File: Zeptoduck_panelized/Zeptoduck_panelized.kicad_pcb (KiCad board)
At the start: 2 copper layers, 23.9 x 37 mm, 110 parts, among them J2 USB4151-GF-C, U1 ATSAMD11D14A-U, U2 TLV73333PDQNR

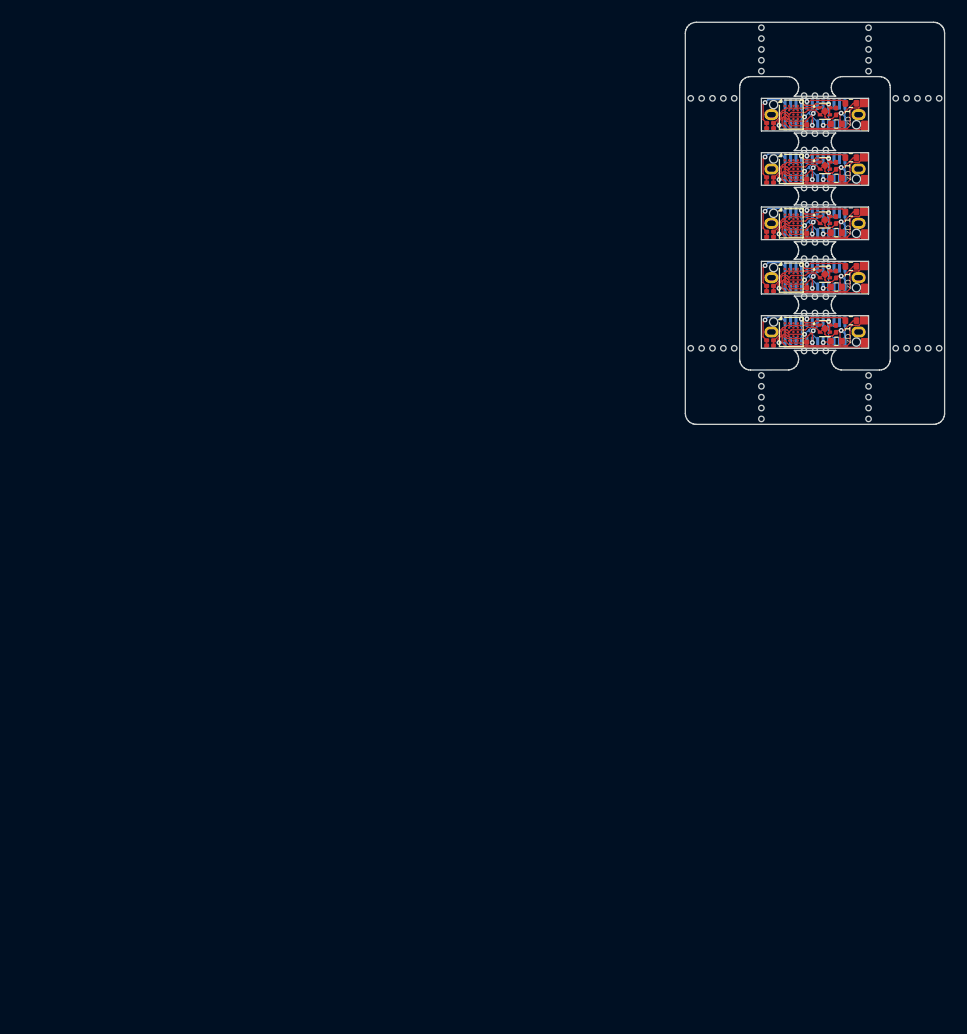
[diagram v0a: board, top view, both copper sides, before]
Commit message: Updated and fixed the Panelization
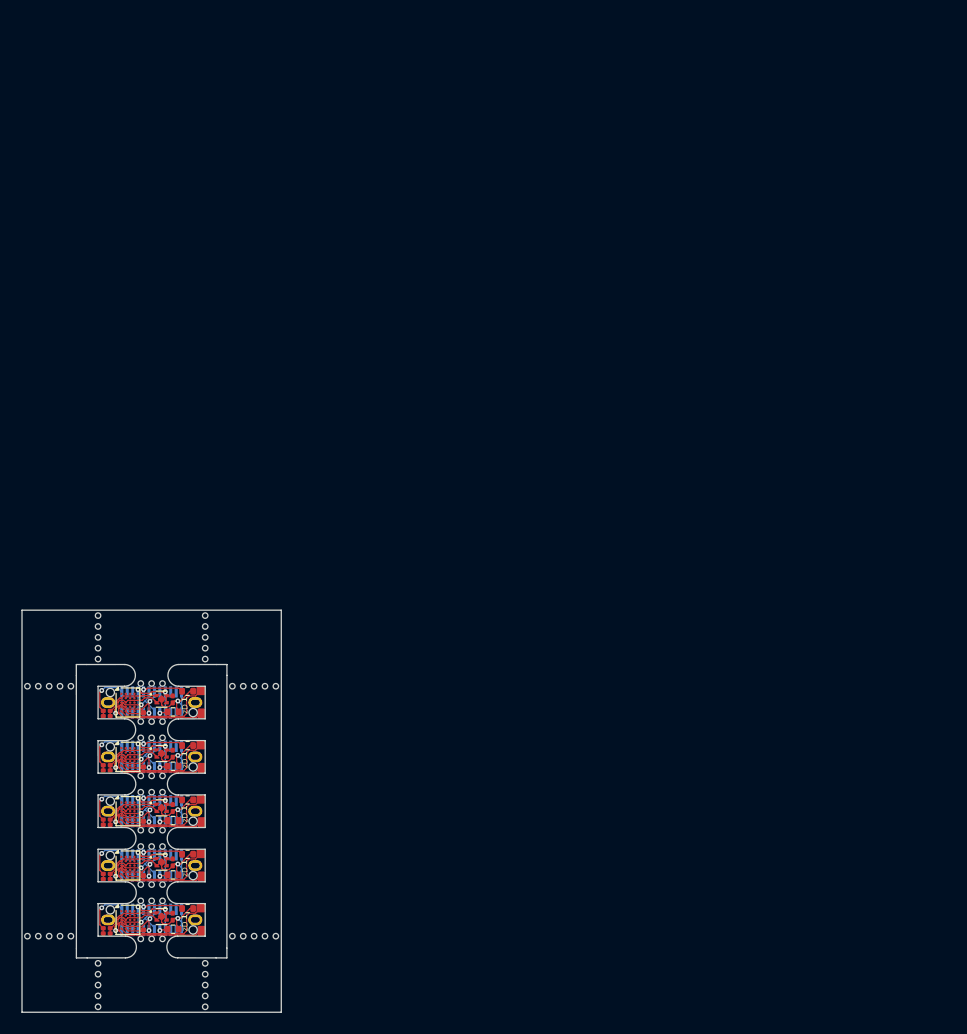
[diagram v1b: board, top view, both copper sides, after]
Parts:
- moved C3 81.6 mm to (83.3, 93.4)
- moved C3 81.6 mm to (83.3, 88.4)
- moved C3 81.6 mm to (83.3, 103.4)
- moved C3 81.6 mm to (83.3, 83.4)
- moved C3 81.6 mm to (83.3, 98.4)
- moved R2 81.6 mm to (90.8, 91.6)
- moved R2 81.6 mm to (90.8, 101.6)
- moved R2 81.6 mm to (90.8, 81.6)
- moved R2 81.6 mm to (90.8, 96.6)
- moved R2 81.6 mm to (90.8, 86.6)
- moved C1 81.6 mm to (83.3, 98.8)
- moved C1 81.6 mm to (83.3, 93.8)
- moved C1 81.6 mm to (83.3, 103.8)
- moved C1 81.6 mm to (83.3, 83.8)
- moved C1 81.6 mm to (83.3, 88.8)
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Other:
- outline, holes or cut-outs redrawn
